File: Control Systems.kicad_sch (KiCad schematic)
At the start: 13 parts, among them SW1 SW_SPDT, U1 STM32F446RETx

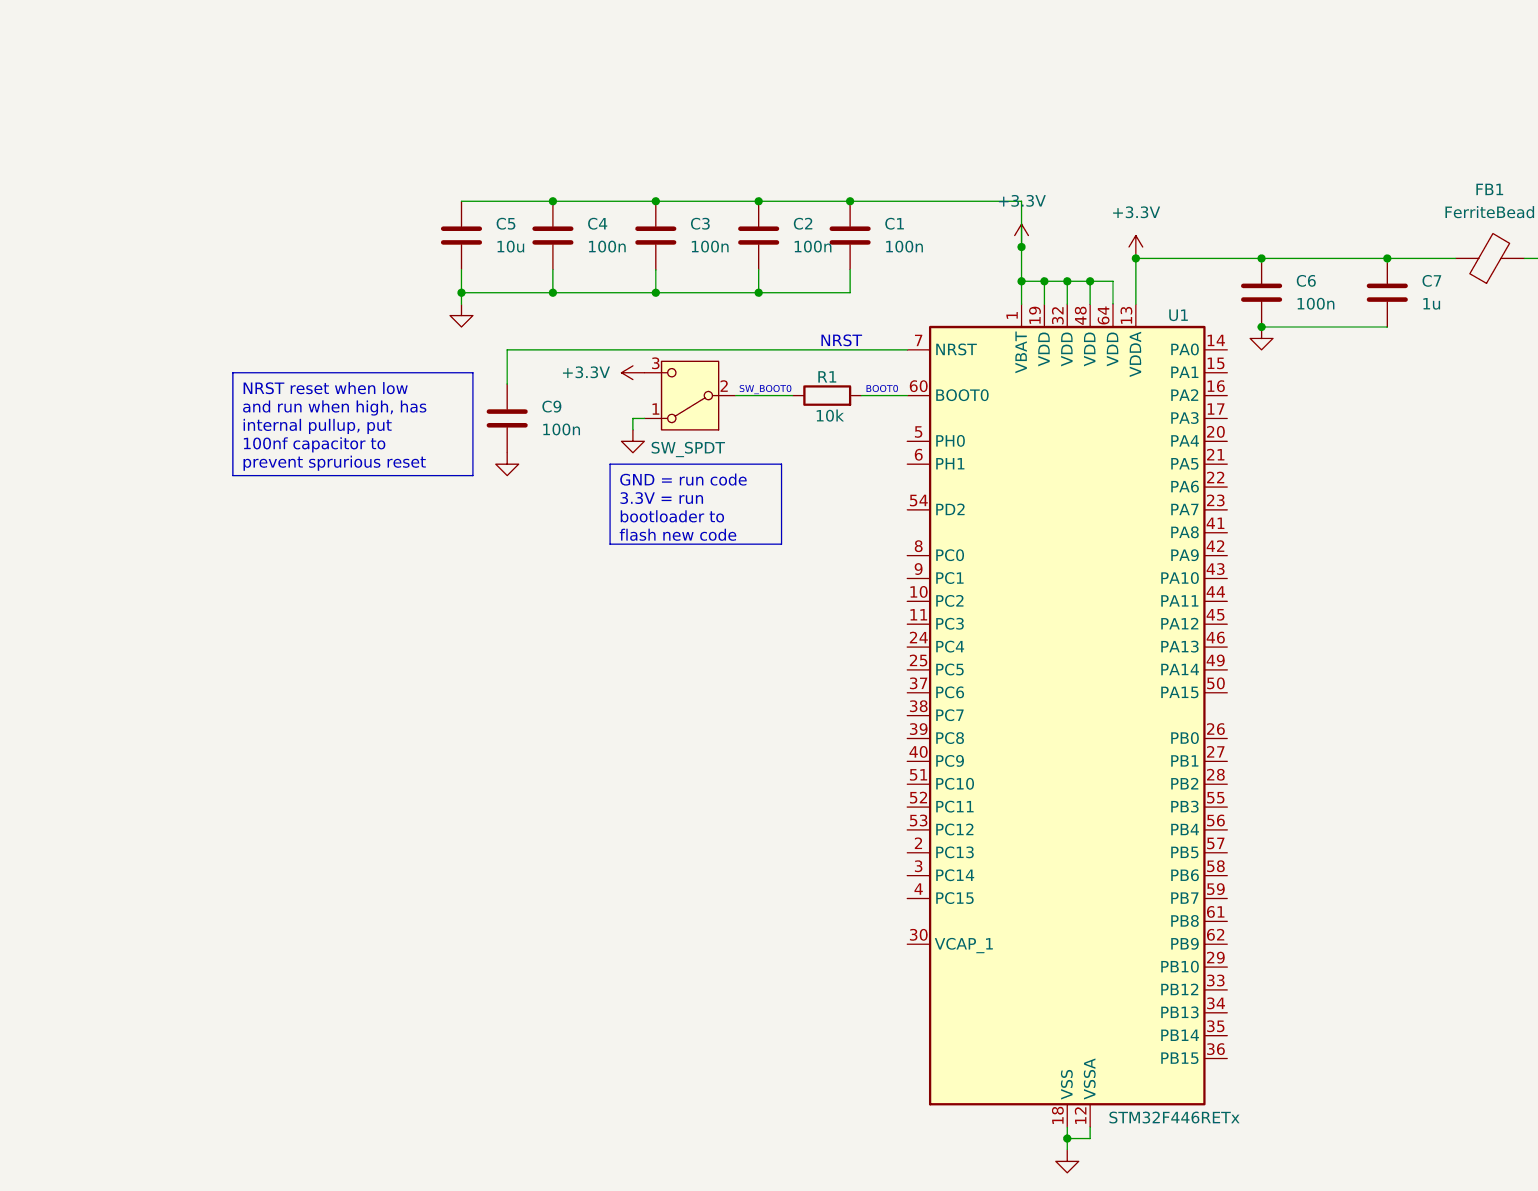
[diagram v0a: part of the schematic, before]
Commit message: feat: added SWD and SDO and apply pins to connect to ST-LINK pins (#1)
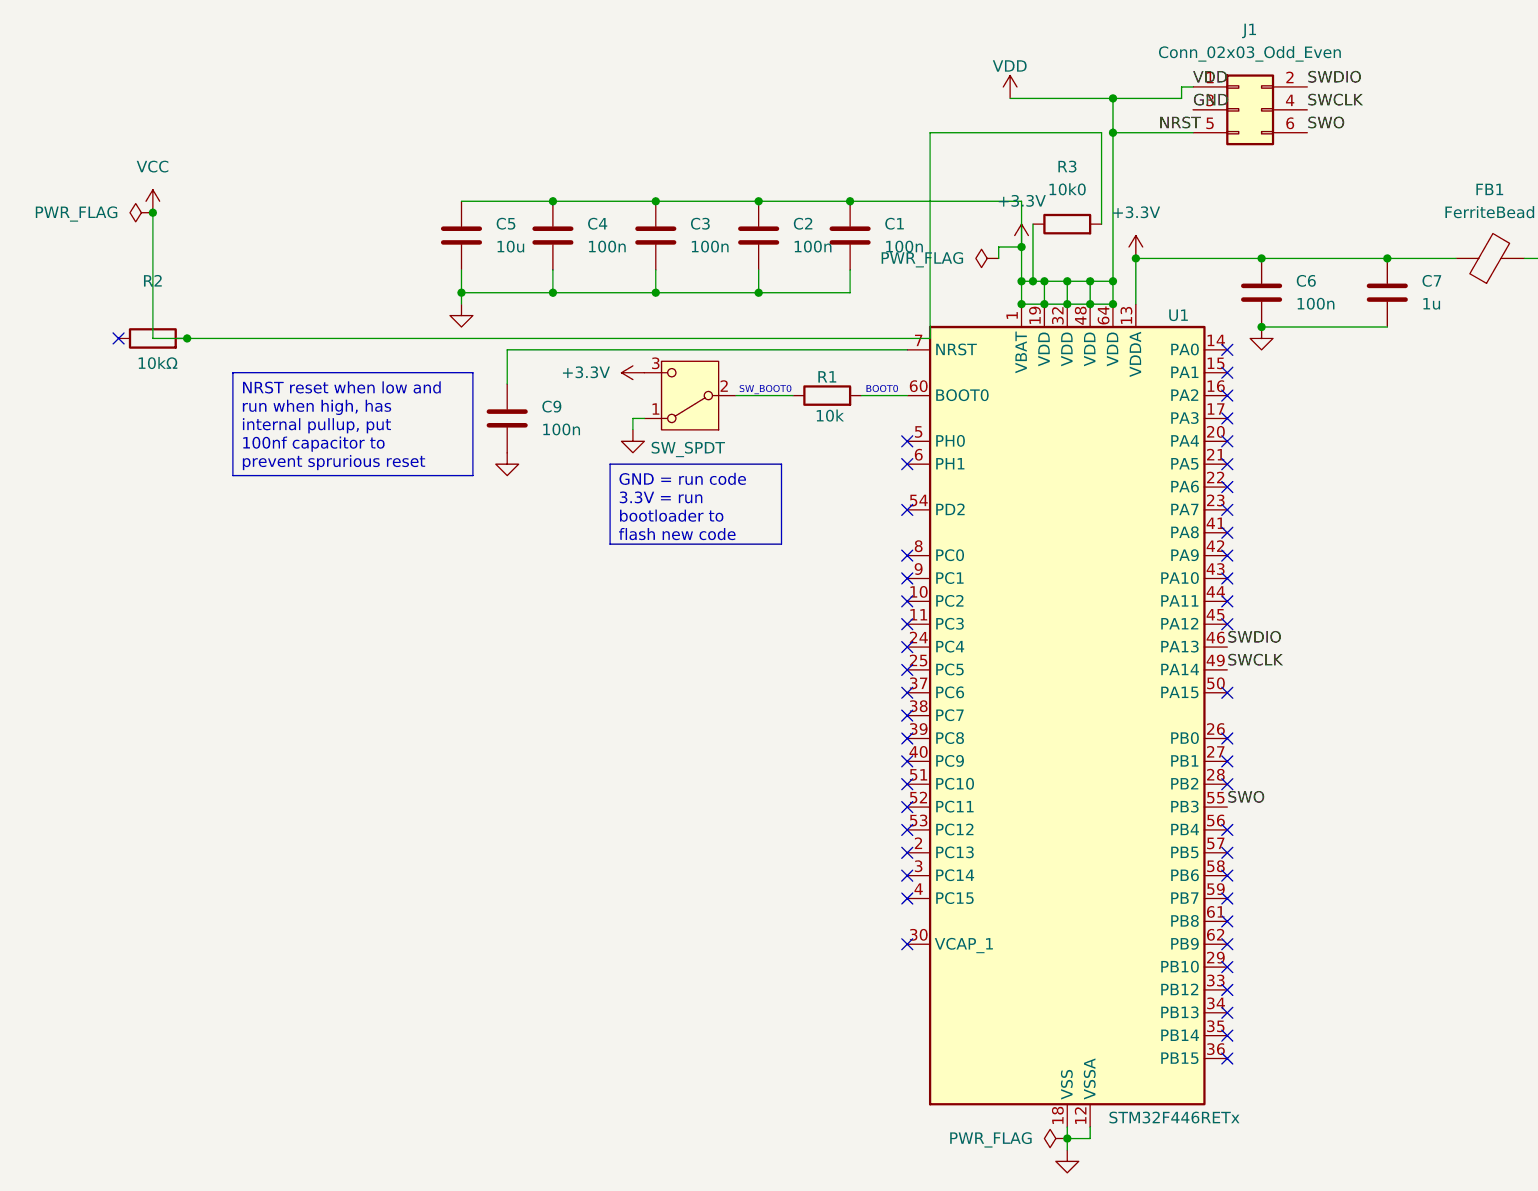
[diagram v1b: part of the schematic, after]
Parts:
- added J1: Conn_02x03_Odd_Even, symbol Connector_Generic:Conn_02x03_Odd_Even
- added R2: 10kΩ, symbol Device:R
- added R3: 10k0, symbol Device:R
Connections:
- net +3.3V: now also J1.1 (Pin_1), J1.5 (Pin_5), R3.1
- net GND: now also J1.3 (Pin_3)
- net SWDIO: now reaches U1.46 (PA13)
- net SWDIO: now also J1.2 (Pin_2)
- net SWCLK: now reaches U1.49 (PA14)
- net SWCLK: now also J1.4 (Pin_4)
- net SWO: now reaches U1.55 (PB3)
- net SWO: now also J1.6 (Pin_6)
- new net VCC: R2.2, R3.2
- no-connect marks 0 -> 49
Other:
- note removed: "NRST"

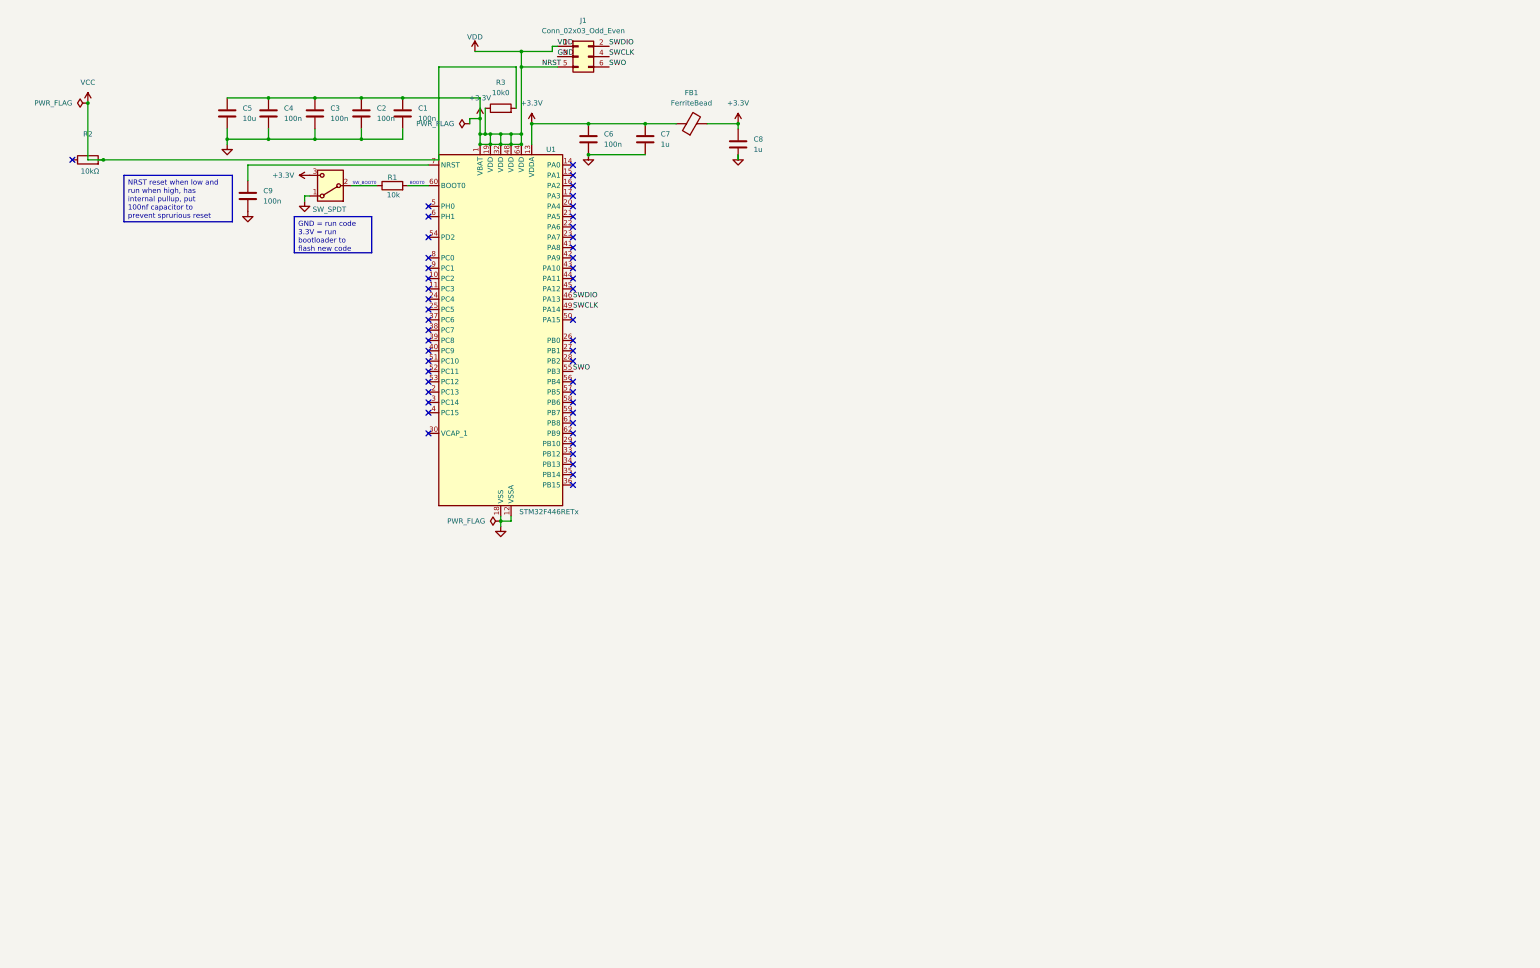
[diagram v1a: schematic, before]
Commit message: Feat: Added wiring for the MCU for 4 components
- added almost all passive components
- added ports for PWM headers 
- wired the main IMU, mag and barometer
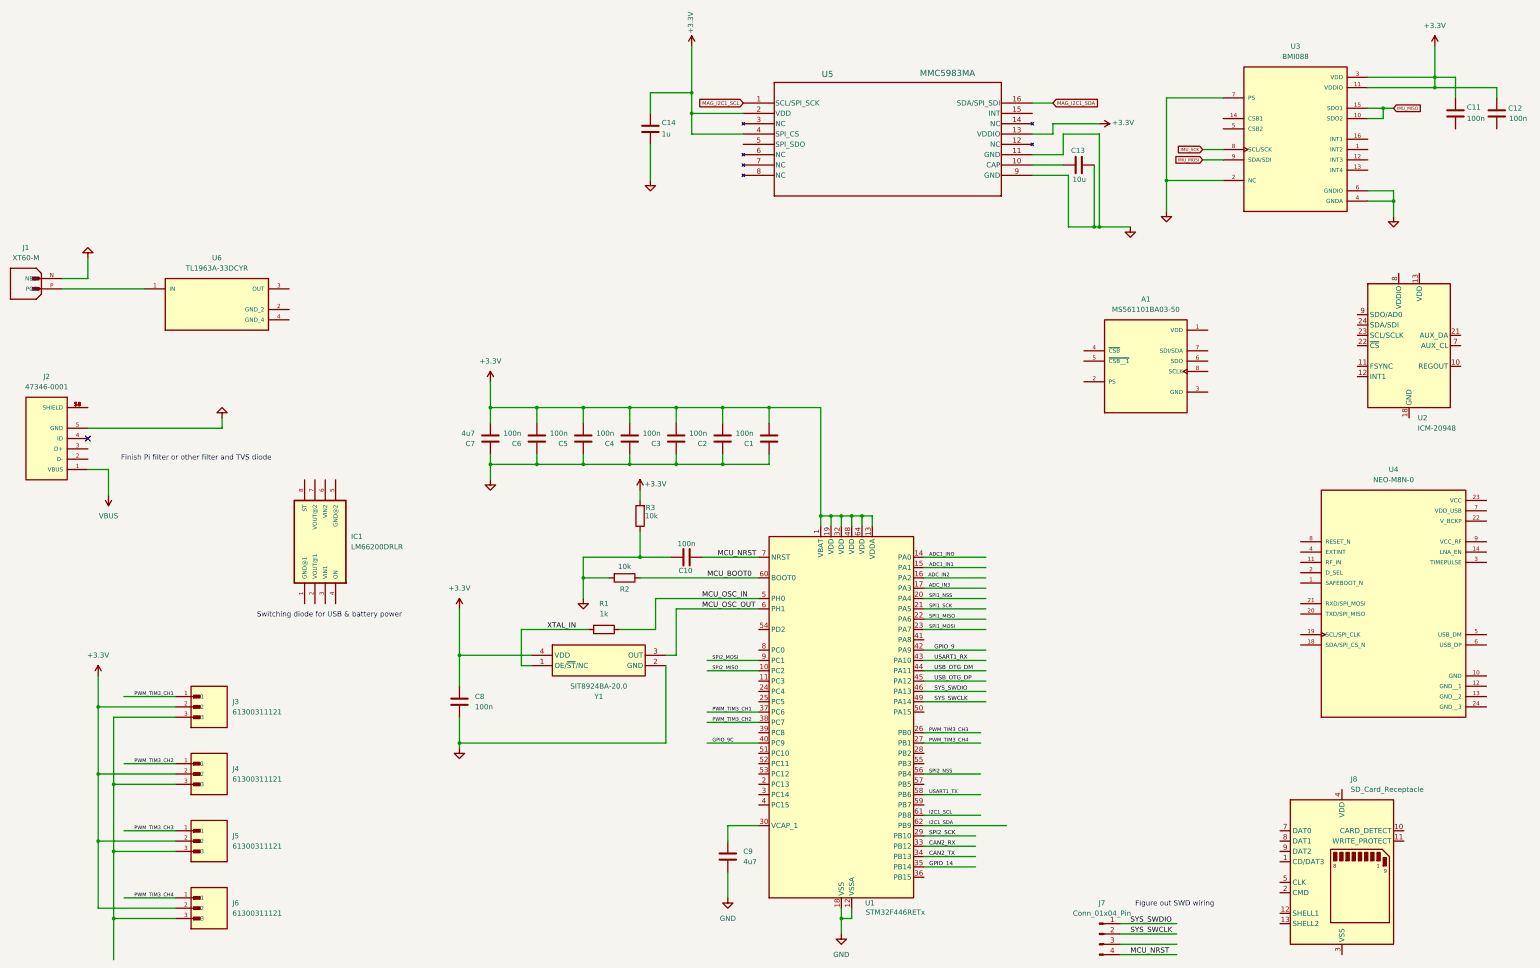
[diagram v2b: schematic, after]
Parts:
- removed FB1: FerriteBead, symbol Device:FerriteBead
- removed J1: Conn_02x03_Odd_Even, symbol Connector_Generic:Conn_02x03_Odd_Even
- removed SW1: SW_SPDT, symbol Switch:SW_SPDT
- added A1: MS561101BA03-50, MS561101BA03-50:XDCR_MS561101BA03-50, symbol MS561101BA03-50:MS561101BA03-50
- added C10, C11, C12: 100n, symbol Device:C
- added C13: 10u, symbol Device:C
- added C14: 1u, symbol Device:C
- added IC1: LM66200DRLR, LM66200DRLR:SOT8, symbol LM66200DRLR:LM66200DRLR
- added J1: XT60-M, XT60-M:AMASS_XT60-M, symbol XT60-M:XT60-M
- added J2: 47346-0001, 47346-0001:MOLEX_47346-0001, symbol 47346-0001:47346-0001
- added J3, J4, J5, J6: 61300311121, 61300311121:WURTH_61300311121, symbol 61300311121:61300311121
- added J7: Conn_01x04_Pin, symbol Connector:Conn_01x04_Pin
- added J8: SD_Card_Receptacle, symbol Connector:SD_Card_Receptacle
- added U2: ICM-20948, Sensor_Motion:InvenSense_QFN-24_3x3mm_P0.4mm, symbol Sensor_Motion:ICM-20948
- added U3: BMI088, BMI088:PQFN50P450X300X100-16N, symbol BMI088:BMI088
- added U4: NEO-M8N-0, NEO-M8N-0:XCVR_NEO-M8N-0, symbol NEO-M8N-0:NEO-M8N-0
- added U5: MMC5983MA, MMC5983MA_MEM, symbol 2025-11-07_18-39-49:MMC5983MA
- added U6: TL1963A-33DCYR, TL1963A-33DCYR:VREG_TL1963A-33DCYR, symbol TL1963A-33DCYR:TL1963A-33DCYR
- added Y1: SIT8924BA-20.0, QFN_3225_4pins, symbol SIT8924BA-22-33E-20_000000:SIT8924BA-22-33E-20.000000
- C5: value 10u -> 100n
- C7: value 1u -> 4u7
- C8: value 1u -> 100n
- C9: value 100n -> 4u7
- R1: value 10k -> 1k
- R2: value 10kΩ -> 10k
- R3: value 10k0 -> 10k
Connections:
- net +3.3V: now also C1.2, C2.2, C3.2, C4.2, C5.2, C6.2, C7.2, R3.2, C11.1, C12.1, C14.1, J3.2, J4.2, J5.2, J6.2, U3.11 (VDDIO), U3.3 (VDD), U5.13 (VDDIO), U5.2 (VDD), U5.4 (SPI_CS), Y1.4 (VDD); no longer C1.1, C2.1, C3.1, C4.1, C5.1, C6.1, C7.1, R3.1
- net GND: no longer C1.2, C2.2, C3.2, C4.2, C5.2, C6.2, C7.2, C8.2
- net MCU_OSC_IN: now reaches R1.1
- net MCU_OSC_IN: now also U1.5 (PH0)
- net MCU_BOOT0: now reaches U1.60 (BOOT0)
- net MCU_BOOT0: now also R2.1; no longer R1.2
- net SPI2_MISO: now reaches U1.10 (PC2)
- net ADC1_INO: now reaches U1.14 (PA0)
- net ADC1_IN1: now reaches U1.15 (PA1)
- net ADC_IN2: now reaches U1.16 (PA2)
- net ADC_IN3: now reaches U1.17 (PA3)
- net SPI1_NSS: now reaches U1.20 (PA4)
- net SPI1_SCK: now reaches U1.21 (PA5)
- net SPI1_MISO: now reaches U1.22 (PA6)
- net SPI1_MOSI: now reaches U1.23 (PA7)
- net PWM_TIM3_CH3: now reaches U1.26 (PB0)
- net PWM_TIM3_CH3: now also J5.1
- net PWM_TIM3_CH4: now reaches U1.27 (PB1)
- net PWM_TIM3_CH4: now also J6.1
- net SPI2_SCK: now reaches U1.29 (PB10)
- net at U1.30 (VCAP_1): now also C9.1
- net CAN2_RX: now reaches U1.33 (PB12)
- net CAN2_TX: now reaches U1.34 (PB13)
- net GPIO_14: now reaches U1.35 (PB14)
- net PWM_TIM3_CH1: now reaches U1.37 (PC6)
- net PWM_TIM3_CH1: now also J3.1
- net PWM_TIM3_CH2: now reaches U1.38 (PC7)
- net PWM_TIM3_CH2: now also J4.1
- net GPIO_9C: now reaches U1.40 (PC9)
- net GPIO_9: now reaches U1.42 (PA9)
- net USART1_RX: now reaches U1.43 (PA10)
- net USB_OTG_DM: now reaches U1.44 (PA11)
- net USB_OTG_DP: now reaches U1.45 (PA12)
- net SPI2_NSS: now reaches U1.56 (PB4)
- net USART1_TX: now reaches U1.58 (PB6)
- net MCU_OSC_OUT: now reaches U1.6 (PH1)
- net MCU_OSC_OUT: now also Y1.3 (OUT)
- net I2C1_SCL: now reaches U1.61 (PB8)
- net I2C1_SDA: now reaches U1.62 (PB9)
- net MCU_NRST: now reaches U1.7 (NRST)
- net MCU_NRST: now also C10.2, J7.4 (Pin_4); no longer C9.1
- net SPI2_MOSI: now reaches U1.9 (PC1)
- net SWCLK renamed SYS_SWCLK
- net SYS_SWCLK: now also J7.2 (Pin_2)
- net SWDIO renamed SYS_SWDIO
- net SYS_SWDIO: now also J7.1 (Pin_1)
- net SWO: no longer names the net of U1.55 (PB3)
- net VCC: no longer names the net of R2.2
- net VCC: now also R3.1, C10.1; no longer R3.2
- new net: C13.1, U5.10 (CAP)
- new net: C13.2, U5.11 (GND), U5.9 (GND)
- new net: C1.1, C2.1, C3.1, C4.1, C5.1, C6.1, C7.1
- new net: J3.3, J4.3, J5.3, J6.3
- new net: J1.P (POS), U6.1 (IN)
- new net: J8.3 (VSS), J8.6 (VSS)
- new net: U3.2 (NC), U3.7 (PS)
- new net: U3.4 (GNDA), U3.6 (GNDIO)
- new net: C8.2, Y1.2 (GND)
- new net: U2.18 (GND), U2.20 (GND)
- new net: J2.S1 (SHIELD), J2.S2 (SHIELD), J2.S3 (SHIELD), J2.S4 (SHIELD), J2.S5 (SHIELD), J2.S6 (SHIELD)
- new net IMU_MISO: U3.10 (SDO2), U3.15 (SDO1)
- new net IMU_MOSI: U3.9 (SDA/SDI)
- new net IMU_SCK: U3.8 (SCL/SCK)
- new net MAG_I2C1_SCL: U5.1 (SCL/SPI_SCK)
- new net MAG_I2C1_SDA: U5.16 (SDA/SPI_SDI)
- new net VBUS: J2.1 (VBUS)
- new net XTAL_IN: R1.2, Y1.1 (OE/~{ST}/NC)
- no-connect marks 49 -> 1
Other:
- note added: "Figure out SWD wiring"
- note added: "Finish Pi filter or other filter and TVS diode"
- note added: "Switching diode for USB & battery power"
- note removed: "BOOT0"
- note removed: "SW_BOOT0"
